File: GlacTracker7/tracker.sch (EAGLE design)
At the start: 87 parts, among them J1 THING_PLUS_PHYSICAL, Q1 2N3906, Q2 DMG6602SVT, Q3 DMG6602SVT, Q6 MMBT3906LT1SMD, Q7 DMG6602SVT, U1 ADXL343BCCZ-RL7, U2 FONA-800-BREAKOUT, U3 MP2155GQ-Z, U4 SPARKFUN-SWARM-M138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

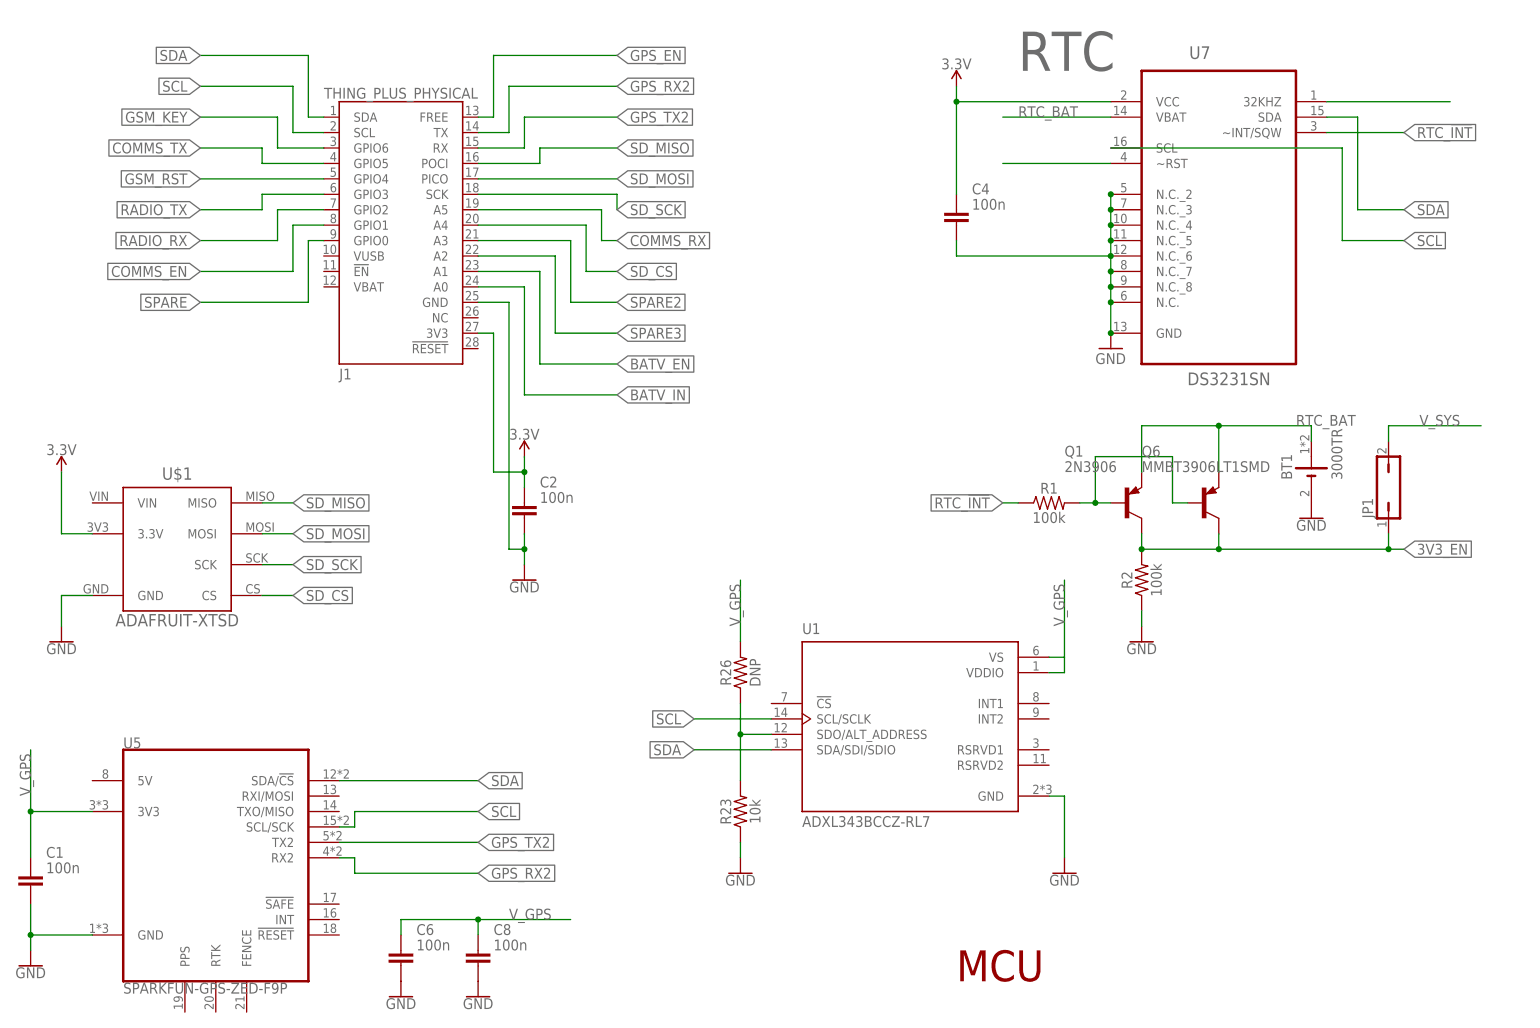
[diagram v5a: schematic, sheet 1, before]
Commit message: Change Key to be grounded and add an Admin pinheader for a button
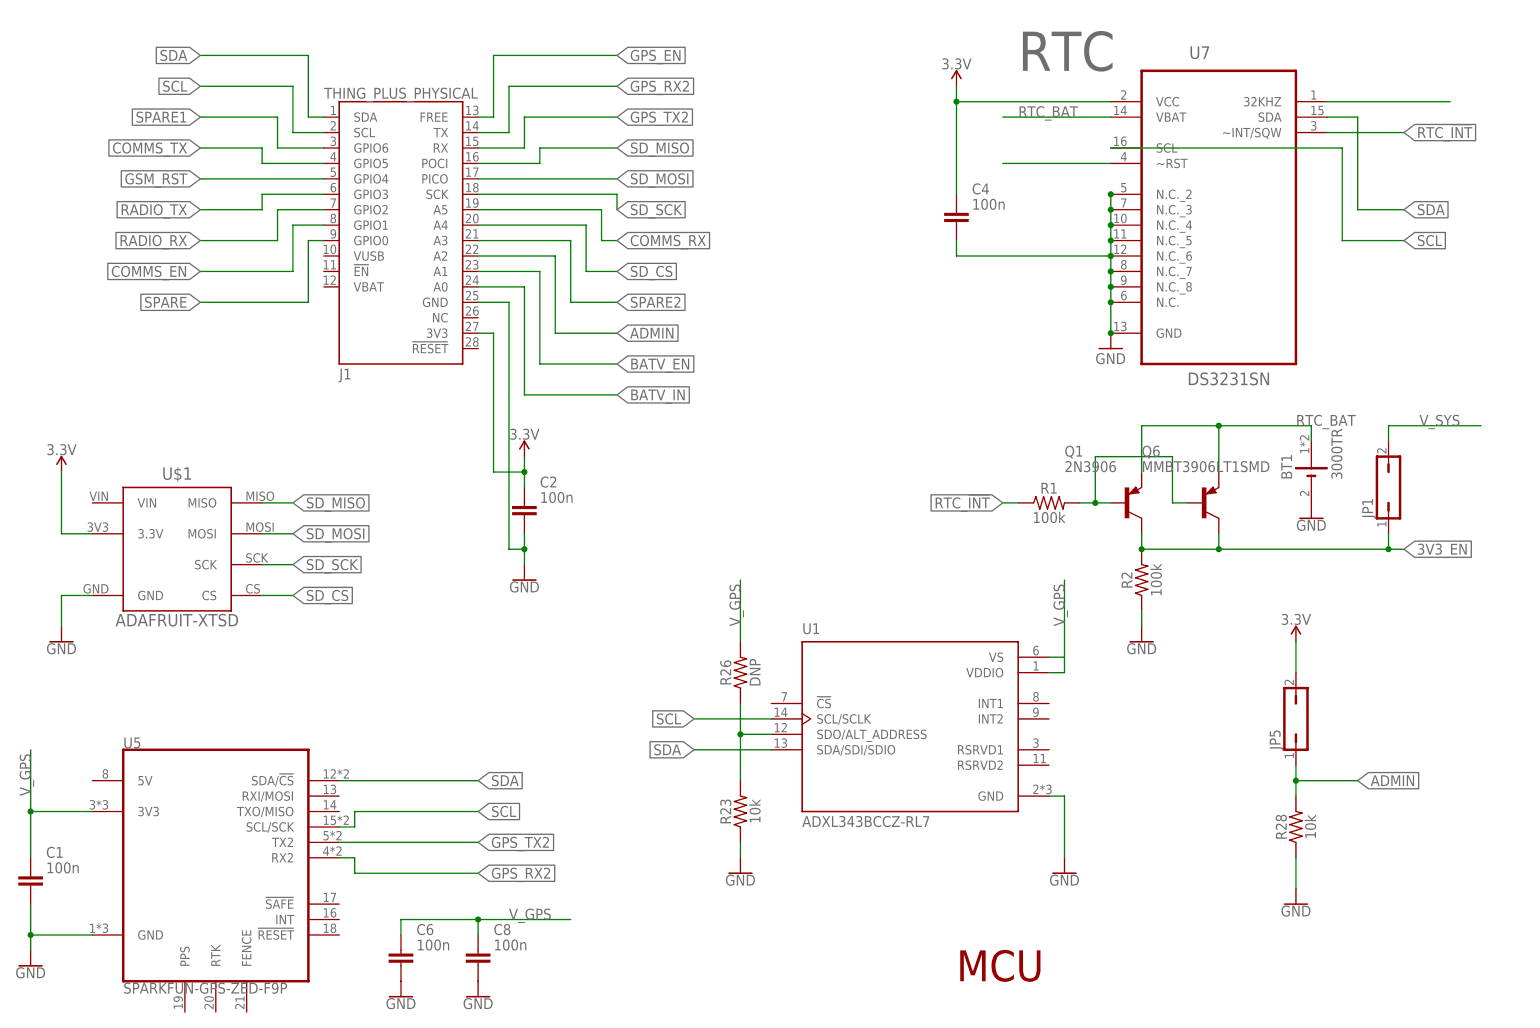
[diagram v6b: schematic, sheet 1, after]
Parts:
- added JP4: JUMPER-SMT_2_NC_TRACE_SILK, SparkFun-Jumpers:JUMPER-SMT_2_NC_TRACE_SILK
- added JP5: (no value), jumper:JP1Q
- added R28: 10k, SparkFun-Resistors:RESISTOR0603
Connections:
- removed net SPARE3: J1.A2
- new net ADMIN: J1.A2, JP5.1, R28.2
- new net SPARE1: J1.GPIO6
- net 3.3V: now also JP5.2
- net GND: now also JP4.2, R28.1
- net GSM_KEY: now also JP4.1; no longer J1.GPIO6
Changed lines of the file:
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@@
 <part name="GND14" library="SparkFun-PowerSymbols" deviceset="GND" device=""/>
 <part name="R26" library="SparkFun-Resistors" deviceset="RESISTOR" device="0603" value="DNP"/>
+<part name="JP4" library="SparkFun-Jumpers" deviceset="JUMPER-SMT_2_NC_TRACE" device="_SILK"/>
+<part name="GND27" library="SparkFun-PowerSymbols" deviceset="GND" device=""/>
+<part name="JP5" library="jumper" deviceset="JP1Q" device=""/>
+<part name="R28" library="SparkFun-Resistors" deviceset="RESISTOR" device="0603" value="10k"/>
+<part name="SUPPLY5" library="SparkFun-PowerSymbols" deviceset="3.3V" device=""/>
+<part name="GND38" library="SparkFun-PowerSymbols" deviceset="GND" device=""/>
 </parts>
 <sheets>
@@
 <attribute name="VALUE" x="131.064" y="66.04" size="1.778" layer="96" font="vector" rot="R90" align="top-center"/>
 </instance>
+<instance part="JP5" gate="A" x="220.98" y="58.42" smashed="yes">
+<attribute name="NAME" x="218.44" y="53.34" size="1.778" layer="95" rot="R90"/>
+<attribute name="VALUE" x="225.425" y="53.34" size="1.778" layer="96" rot="R90"/>
+</instance>
+<instance part="R28" gate="G$1" x="220.98" y="40.64" smashed="yes" rot="R90">
+<attribute name="NAME" x="219.456" y="40.64" size="1.778" layer="95" font="vector" rot="R90" align="bottom-center"/>
+<attribute name="VALUE" x="222.504" y="40.64" size="1.778" layer="96" font="vector" rot="R90" align="top-center"/>
+</instance>
+<instance part="SUPPLY5" gate="G$1" x="220.98" y="71.12" smashed="yes">
+<attribute name="VALUE" x="220.98" y="73.914" size="1.778" layer="96" align="bottom-center"/>
+</instance>
+<instance part="GND38" gate="1" x="220.98" y="27.94" smashed="yes">
+<attribute name="VALUE" x="220.98" y="27.686" size="1.778" layer="96" align="top-center"/>
+</instance>
 </instances>
 <busses>
@@
 <pinref part="SUPPLY1" gate="G$1" pin="3.3V"/>
 <wire x1="17.78" y1="88.9" x2="17.78" y2="99.06" width="0.1524" layer="91"/>
+</segment>
+<segment>
+<pinref part="JP5" gate="A" pin="2"/>
+<pinref part="SUPPLY5" gate="G$1" pin="3.3V"/>
+<wire x1="220.98" y1="66.04" x2="220.98" y2="71.12" width="0.1524" layer="91"/>
 </segment>
 </net>
@@
 <wire x1="182.88" y1="45.72" x2="182.88" y2="35.56" width="0.1524" layer="91"/>
 </segment>
+<segment>
+<pinref part="GND38" gate="1" pin="GND"/>
+<pinref part="R28" gate="G$1" pin="1"/>
+<wire x1="220.98" y1="30.48" x2="220.98" y2="35.56" width="0.1524" layer="91"/>
+</segment>
 </net>
 <net name="RADIO_TX" class="0">
@@
 </segment>
 </net>
-<net name="GSM_KEY" class="0">
-<segment>
-<label x="40.64" y="157.48" size="1.778" layer="95" rot="MR0" xref="yes"/>
-<wire x1="53.34" y1="152.4" x2="53.34" y2="157.48" width="0.1524" layer="91"/>
-<wire x1="53.34" y1="157.48" x2="40.64" y2="157.48" width="0.1524" layer="91"/>
-<pinref part="J1" gate="G$1" pin="GPIO6"/>
-<wire x1="60.96" y1="152.4" x2="53.34" y2="152.4" width="0.1524" layer="91"/>
-</segment>
-</net>
 <net name="BATV_EN" class="0">
 <segment>
@@
 </segment>
 </net>
-<net name="SPARE3" class="0">
+<net name="ADMIN" class="0">
 <segment>
 <wire x1="99.06" y1="121.92" x2="109.22" y2="121.92" width="0.1524" layer="91"/>
@@
 <wire x1="86.36" y1="134.62" x2="99.06" y2="134.62" width="0.1524" layer="91"/>
 <wire x1="99.06" y1="134.62" x2="99.06" y2="121.92" width="0.1524" layer="91"/>
+</segment>
+<segment>
+<wire x1="220.98" y1="48.26" x2="231.14" y2="48.26" width="0.1524" layer="91"/>
+<label x="231.14" y="48.26" size="1.778" layer="95" xref="yes"/>
+<pinref part="R28" gate="G$1" pin="2"/>
+<pinref part="JP5" gate="A" pin="1"/>
+<wire x1="220.98" y1="45.72" x2="220.98" y2="48.26" width="0.1524" layer="91"/>
+<junction x="220.98" y="48.26"/>
+<wire x1="220.98" y1="48.26" x2="220.98" y2="50.8" width="0.1524" layer="91"/>
 </segment>
 </net>
@@
 <wire x1="129.54" y1="55.88" x2="129.54" y2="60.96" width="0.1524" layer="91"/>
 <junction x="129.54" y="55.88"/>
+</segment>
+</net>
+<net name="SPARE1" class="0">
+<segment>
+<label x="40.64" y="157.48" size="1.778" layer="95" rot="MR0" xref="yes"/>
+<wire x1="53.34" y1="152.4" x2="53.34" y2="157.48" width="0.1524" layer="91"/>
+<wire x1="53.34" y1="157.48" x2="40.64" y2="157.48" width="0.1524" layer="91"/>
+<pinref part="J1" gate="G$1" pin="GPIO6"/>
+<wire x1="60.96" y1="152.4" x2="53.34" y2="152.4" width="0.1524" layer="91"/>
 </segment>
 </net>
@@
 </instance>
 <instance part="XB1" gate="G$1" x="33.02" y="137.16" rot="MR0"/>
-<instance part="GND7" gate="1" x="154.94" y="58.42" smashed="yes" rot="MR0">
-<attribute name="VALUE" x="154.94" y="58.166" size="1.778" layer="96" rot="MR0" align="top-center"/>
+<instance part="GND7" gate="1" x="154.94" y="53.34" smashed="yes" rot="MR0">
+<attribute name="VALUE" x="154.94" y="53.086" size="1.778" layer="96" rot="MR0" align="top-center"/>
 </instance>
 <instance part="U2" gate="G$1" x="182.88" y="71.12" smashed="yes">
@@
 <attribute name="NAME" x="40.64" y="17.78" size="1.778" layer="95" rot="R90"/>
 <attribute name="VALUE" x="47.625" y="17.78" size="1.778" layer="96" rot="R90"/>
+</instance>
+<instance part="JP4" gate="G$1" x="203.2" y="63.5" smashed="yes" rot="R270">
+<attribute name="NAME" x="205.74" y="66.04" size="1.778" layer="95" font="vector" rot="R270"/>
+</instance>
+<instance part="GND27" gate="1" x="203.2" y="53.34" smashed="yes" rot="MR0">
+<attribute name="VALUE" x="203.2" y="53.086" size="1.778" layer="96" rot="MR0" align="top-center"/>
 </instance>
 </instances>
@@
 <pinref part="GND7" gate="1" pin="GND"/>
 <wire x1="157.48" y1="63.5" x2="154.94" y2="63.5" width="0.1524" layer="91"/>
-<wire x1="154.94" y1="63.5" x2="154.94" y2="60.96" width="0.1524" layer="91"/>
+<wire x1="154.94" y1="63.5" x2="154.94" y2="55.88" width="0.1524" layer="91"/>
 <pinref part="C10" gate="G$1" pin="-"/>
 <wire x1="165.1" y1="66.294" x2="165.1" y2="63.5" width="0.1524" layer="91"/>
@@
 <wire x1="43.18" y1="15.24" x2="43.18" y2="12.7" width="0.1524" layer="91"/>
 </segment>
+<segment>
+<pinref part="GND27" gate="1" pin="GND"/>
+<pinref part="JP4" gate="G$1" pin="2"/>
+<wire x1="203.2" y1="55.88" x2="203.2" y2="58.42" width="0.1524" layer="91"/>
+</segment>
 </net>
 <net name="RADIO_TX" class="0">
@@
 <label x="215.9" y="83.82" size="1.778" layer="95" xref="yes"/>
 <pinref part="U2" gate="G$1" pin="KEY"/>
-<wire x1="200.66" y1="83.82" x2="215.9" y2="83.82" width="0.1524" layer="91"/>
-</segment>
-</net>
+<wire x1="200.66" y1="83.82" x2="203.2" y2="83.82" width="0.1524" layer="91"/>
+<pinref part="JP4" gate="G$1" pin="1"/>
+<wire x1="203.2" y1="83.82" x2="215.9" y2="83.82" width="0.1524" layer="91"/>
+<wire x1="203.2" y1="68.58" x2="203.2" y2="83.82" width="0.1524" layer="91"/>
+<junction x="203.2" y="83.82"/>
+</segment>
+</net>

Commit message: Fix the overlapping holes DRC
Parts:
- added U$2: SLOT130.5, GlacTracker:SLOT130.5
- U2: value FONA-800-BREAKOUT -> FONA-800-BREAKOUTNOHOLE; device GlacTracker:FONA-800-BREAKOUT -> GlacTracker:FONA-800-BREAKOUTNOHOLE
- U4: value SPARKFUN-SWARM-M138 -> SPARKFUN-SWARM-M138NOTOPHOLE; device GlacTracker:SPARKFUN-SWARM-M138 -> GlacTracker:SPARKFUN-SWARM-M138NOTOPHOLE
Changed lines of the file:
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@@
 <parts>
 <part name="FRAME2" library="frames" deviceset="A4L-LOC" device=""/>
-<part name="U4" library="GlacTracker" deviceset="SPARKFUN-SWARM-M138" device=""/>
+<part name="U4" library="GlacTracker" deviceset="SPARKFUN-SWARM-M138" device="NOTOPHOLE" value="SPARKFUN-SWARM-M138NOTOPHOLE"/>
 <part name="U5" library="GlacTracker" deviceset="SPARKFUN-GPS-ZED-F9P" device=""/>
 <part name="J1" library="SparkFun-Boards" deviceset="THING_PLUS_PHYSICAL" device=""/>
@@
 <part name="GND6" library="SparkFun-PowerSymbols" deviceset="GND" device=""/>
 <part name="GND7" library="SparkFun-PowerSymbols" deviceset="GND" device=""/>
-<part name="U2" library="GlacTracker" deviceset="FONA-800-BREAKOUT" device=""/>
+<part name="U2" library="GlacTracker" deviceset="FONA-800-BREAKOUT" device="NOHOLE" value="FONA-800-BREAKOUTNOHOLE"/>
 <part name="Q1" library="transistor-pnp" deviceset="2N3906" device=""/>
 <part name="R1" library="SparkFun-Resistors" deviceset="RESISTOR" device="0603" value="100k"/>
@@
 <part name="SUPPLY5" library="SparkFun-PowerSymbols" deviceset="3.3V" device=""/>
 <part name="GND38" library="SparkFun-PowerSymbols" deviceset="GND" device=""/>
+<part name="U$2" library="GlacTracker" deviceset="SLOT130.5" device=""/>
 </parts>
 <sheets>
@@
 <attribute name="VALUE" x="203.2" y="53.086" size="1.778" layer="96" rot="MR0" align="top-center"/>
 </instance>
+<instance part="U$2" gate="G$1" x="99.06" y="96.52"/>
 </instances>
 <busses>

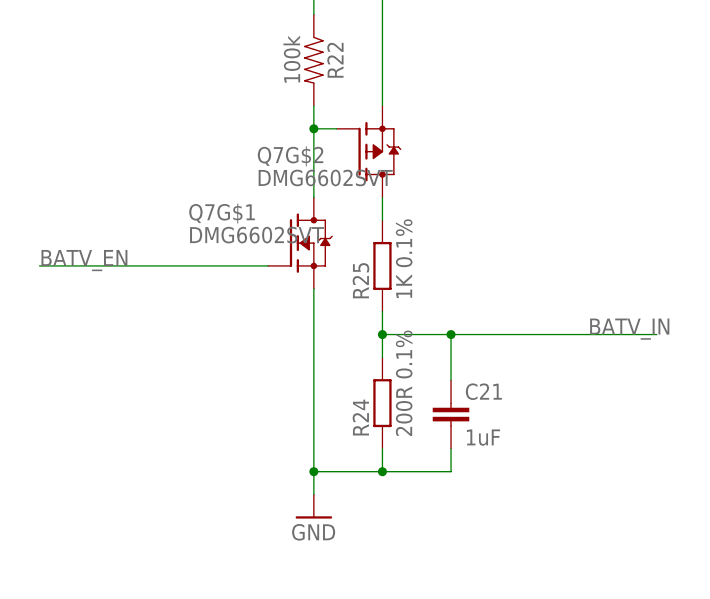
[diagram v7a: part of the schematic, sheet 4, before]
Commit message: Add BatVolts divider values
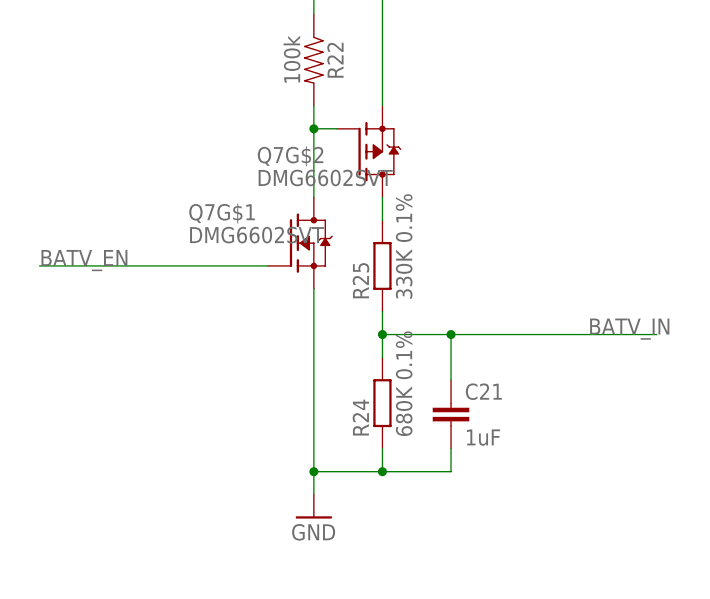
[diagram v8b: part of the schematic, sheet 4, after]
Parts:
- R24: value 200R 0.1% -> 680K 0.1%
- R25: value 1K 0.1% -> 330K 0.1%
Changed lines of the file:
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@@
 <part name="JP2" library="jumper" deviceset="JP1Q" device=""/>
 <part name="Q6" library="transistor-pnp" deviceset="MMBT3906*" device="SMD" technology="LT1"/>
-<part name="R24" library="resistor" deviceset="R-EU_" device="R0805" value="200R 0.1%"/>
-<part name="R25" library="resistor" deviceset="R-EU_" device="R0805" value="1K 0.1%"/>
+<part name="R24" library="resistor" deviceset="R-EU_" device="R0805" value="680K 0.1%"/>
+<part name="R25" library="resistor" deviceset="R-EU_" device="R0805" value="330K 0.1%"/>
 <part name="C21" library="resistor" deviceset="C-EU" device="C0805" value="1uF"/>
 <part name="GND37" library="supply1" deviceset="GND" device=""/>
